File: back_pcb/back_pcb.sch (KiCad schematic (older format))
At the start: 68 parts, among them P1 EXPANSION_LEFT, P2 EXPANSION_BOTTOM, P3 EXPANSION_TOP, P5 AUDIO_CONN, P6 ATMEGA_HEADER, P7 EXPANSION_BOTTOM2, P8 JST, P9 USB_A, Q1 IRLML6401, Q2 IRLML6401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

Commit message: Lots of changes for the Delta revision
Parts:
- removed C15: 100nF, Capacitors_SMD:C_0805_HandSoldering, symbol C_Small
- removed JP5: JUMPER, Connect:GS2, symbol JUMPER
- removed P1: EXPANSION_LEFT, Pin_Headers:Pin_Header_Angled_1x13_Pitch2.54mm, symbol CONN_01X13
- removed P5: AUDIO_CONN, Pin_Headers:Pin_Header_Straight_1x04_Pitch2.54mm, symbol CONN_01X04
- removed W4: TEST_1P, Measurement_Points:Measurement_Point_Square-SMD-Pad_Small, symbol TEST_1P
- added C10, C9: 100nF, common-footprints:C_0805_100nF_HandSoldering, symbol C_Small
- added J1: Conn_01x12, Pin_Headers:Pin_Header_Angled_1x12_Pitch2.54mm, symbol Conn_01x12
- added JP8: WP, common-footprints:GS2_SMALL, symbol JUMPER
- added P4: AUDIO_CONN, Pin_Headers:Pin_Header_Straight_1x06_Pitch2.54mm, symbol CONN_01X06
- added R8: 10K, common-footprints:R_0805_10K_HandSoldering, symbol R
- added U5: 24LC16, Housings_SOIC:SOIC-8_3.9x4.9mm_Pitch1.27mm, symbol 24LC16
- C13, C14, C2, C25, C5, C6, C8: footprint Capacitors_SMD:C_0805_HandSoldering -> common-footprints:C_0805_100nF_HandSoldering
- C4, C7: footprint Capacitors_Tantalum_SMD:CP_Tantalum_Case-B_EIA-3528-21_Hand -> Capacitors_Tantalum_SMD:CP_Tantalum_Case-D_EIA-7343-31_Hand
- P9: symbol USB_A-RESCUE-back_prototype -> USB_A-RESCUE-back_pcb
- R1, R10, R11, R2, R3, R4: footprint Resistors_SMD:R_0805_HandSoldering -> common-footprints:R_0805_10K_HandSoldering
- R5, R6, R7: value 1K -> 47
- U1: footprint common-footprints:pi0outline -> footprints:Pi0-BACK
- U3: symbol MCP23017-RESCUE-back_prototype -> MCP23017-RESCUE-back_pcb
- W25: value TEST_1P -> D-
- W26: value TEST_1P -> D+
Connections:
- net labels added: +3.3VA, AMPLIFIER_ON, BAT_IN+, BAT_IN-
- net labels removed: BATT+, BATT-, IMU_INT, RTC_ALARM
- wire segments 85 -> 99
- no-connect marks 22 -> 24
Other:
- note added: "The board has a cutout,\nyou solder wires from\nthese testpoints to\nPi Zero USB testpoints,\nwires go through\nthe cutout."
- note removed: "The board has a cutout,\nyou solder wires from\nthese testpoints to\nPi USB testpoints,\nwires go through\nthe cutout."
- moved on the sheet: C17, C19, C22, C24, C3, C6, L1, L2, P8, Q2, R4, SW1

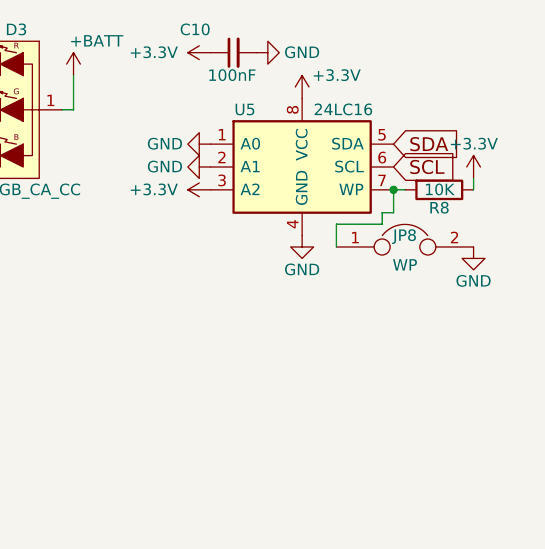
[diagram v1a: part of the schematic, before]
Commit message: Renaming WP (write protect) into WE (write enable)
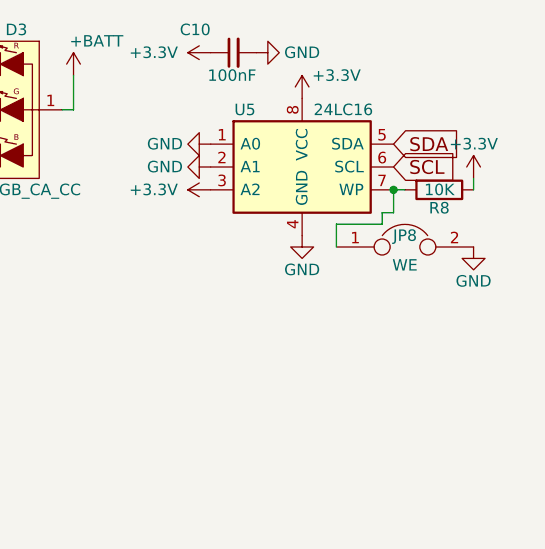
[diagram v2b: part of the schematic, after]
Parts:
- JP8: value WP -> WE
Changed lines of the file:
@@
 P 10800 1450
 F 0 "JP8" H 10800 1500 50  0000 C CNN
-F 1 "WP" H 10800 1370 50  0000 C CNN
+F 1 "WE" H 10800 1370 50  0000 C CNN
 F 2 "common-footprints:GS2_SMALL" H 10800 1450 50  0001 C CNN
 F 3 "" H 10800 1450 50  0000 C CNN

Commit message: More silkscreen changes
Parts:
- Q1, Q2, Q4: footprint TO_SOT_Packages_SMD:SOT-23_Handsoldering -> common-footprints:IRLML6401-SOT-23_Handsoldering
- R5, R6, R7: footprint Resistors_SMD:R_0805_HandSoldering -> common-footprints:R_0805_47R_HandSoldering
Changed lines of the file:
@@
 F 0 "R5" V 8830 650 50  0000 C CNN
 F 1 "47" V 8750 650 50  0000 C CNN
-F 2 "Resistors_SMD:R_0805_HandSoldering" V 8680 650 50  0001 C CNN
+F 2 "common-footprints:R_0805_47R_HandSoldering" V 8680 650 50  0001 C CNN
 F 3 "" H 8750 650 50  0000 C CNN
 	1    8750 650
@@
 F 0 "R6" V 8830 850 50  0000 C CNN
 F 1 "47" V 8750 850 50  0000 C CNN
-F 2 "Resistors_SMD:R_0805_HandSoldering" V 8680 850 50  0001 C CNN
+F 2 "common-footprints:R_0805_47R_HandSoldering" V 8680 850 50  0001 C CNN
 F 3 "" H 8750 850 50  0000 C CNN
 	1    8750 850
@@
 F 0 "R7" V 8830 1050 50  0000 C CNN
 F 1 "47" V 8750 1050 50  0000 C CNN
-F 2 "Resistors_SMD:R_0805_HandSoldering" V 8680 1050 50  0001 C CNN
+F 2 "common-footprints:R_0805_47R_HandSoldering" V 8680 1050 50  0001 C CNN
 F 3 "" H 8750 1050 50  0000 C CNN
 	1    8750 1050
@@
 F 0 "Q1" V 7400 2350 50  0000 R CNN
 F 1 "IRLML6401" V 7650 2350 50  0000 R CNN
-F 2 "TO_SOT_Packages_SMD:SOT-23_Handsoldering" H 7650 2250 50  0001 C CNN
+F 2 "common-footprints:IRLML6401-SOT-23_Handsoldering" H 7650 2250 50  0001 C CNN
 F 3 "" H 7450 2150 50  0000 C CNN
 	1    7450 2150
@@
 F 0 "Q4" V 7850 6500 50  0000 R CNN
 F 1 "IRLML6401" V 8100 6500 50  0000 R CNN
-F 2 "TO_SOT_Packages_SMD:SOT-23_Handsoldering" H 8100 6400 50  0001 C CNN
+F 2 "common-footprints:IRLML6401-SOT-23_Handsoldering" H 8100 6400 50  0001 C CNN
 F 3 "" H 7900 6300 50  0000 C CNN
 	1    7900 6300
@@
 F 0 "Q2" V 7850 3950 50  0000 R CNN
 F 1 "IRLML6401" V 8100 3950 50  0000 R CNN
-F 2 "TO_SOT_Packages_SMD:SOT-23_Handsoldering" H 8100 3850 50  0001 C CNN
+F 2 "common-footprints:IRLML6401-SOT-23_Handsoldering" H 8100 3850 50  0001 C CNN
 F 3 "" H 7900 3750 50  0000 C CNN
 	1    7900 3750

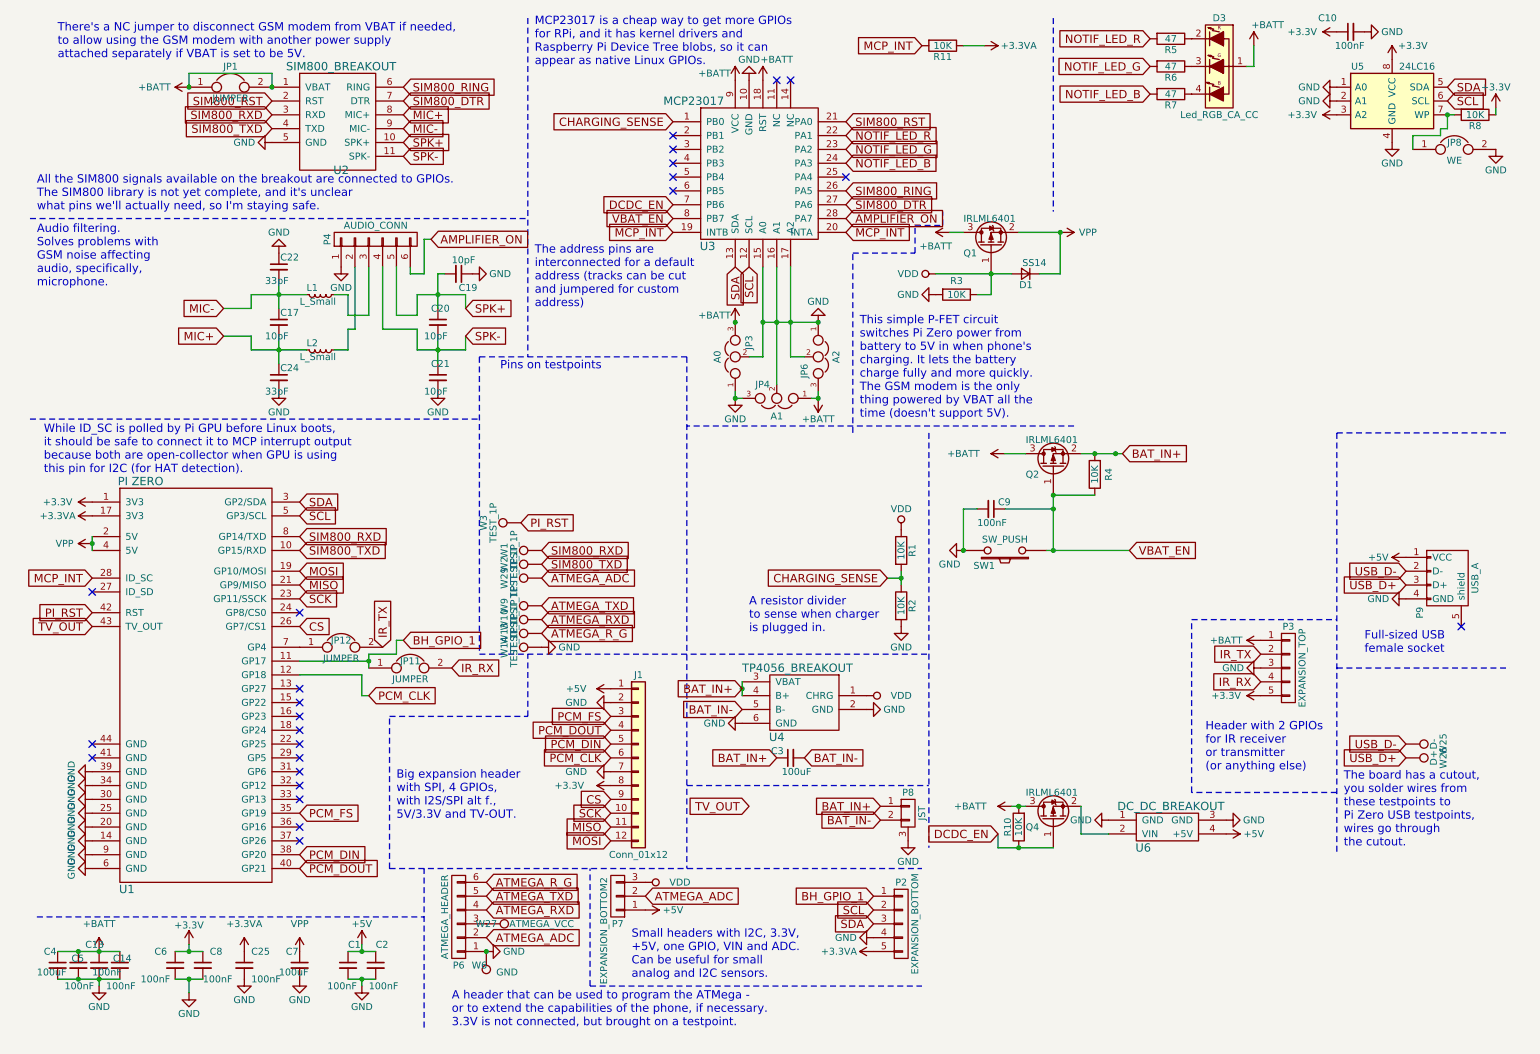
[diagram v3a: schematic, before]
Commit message: Added a UART buffer, TX/RX testpoints, 1N4148 and other silk changes
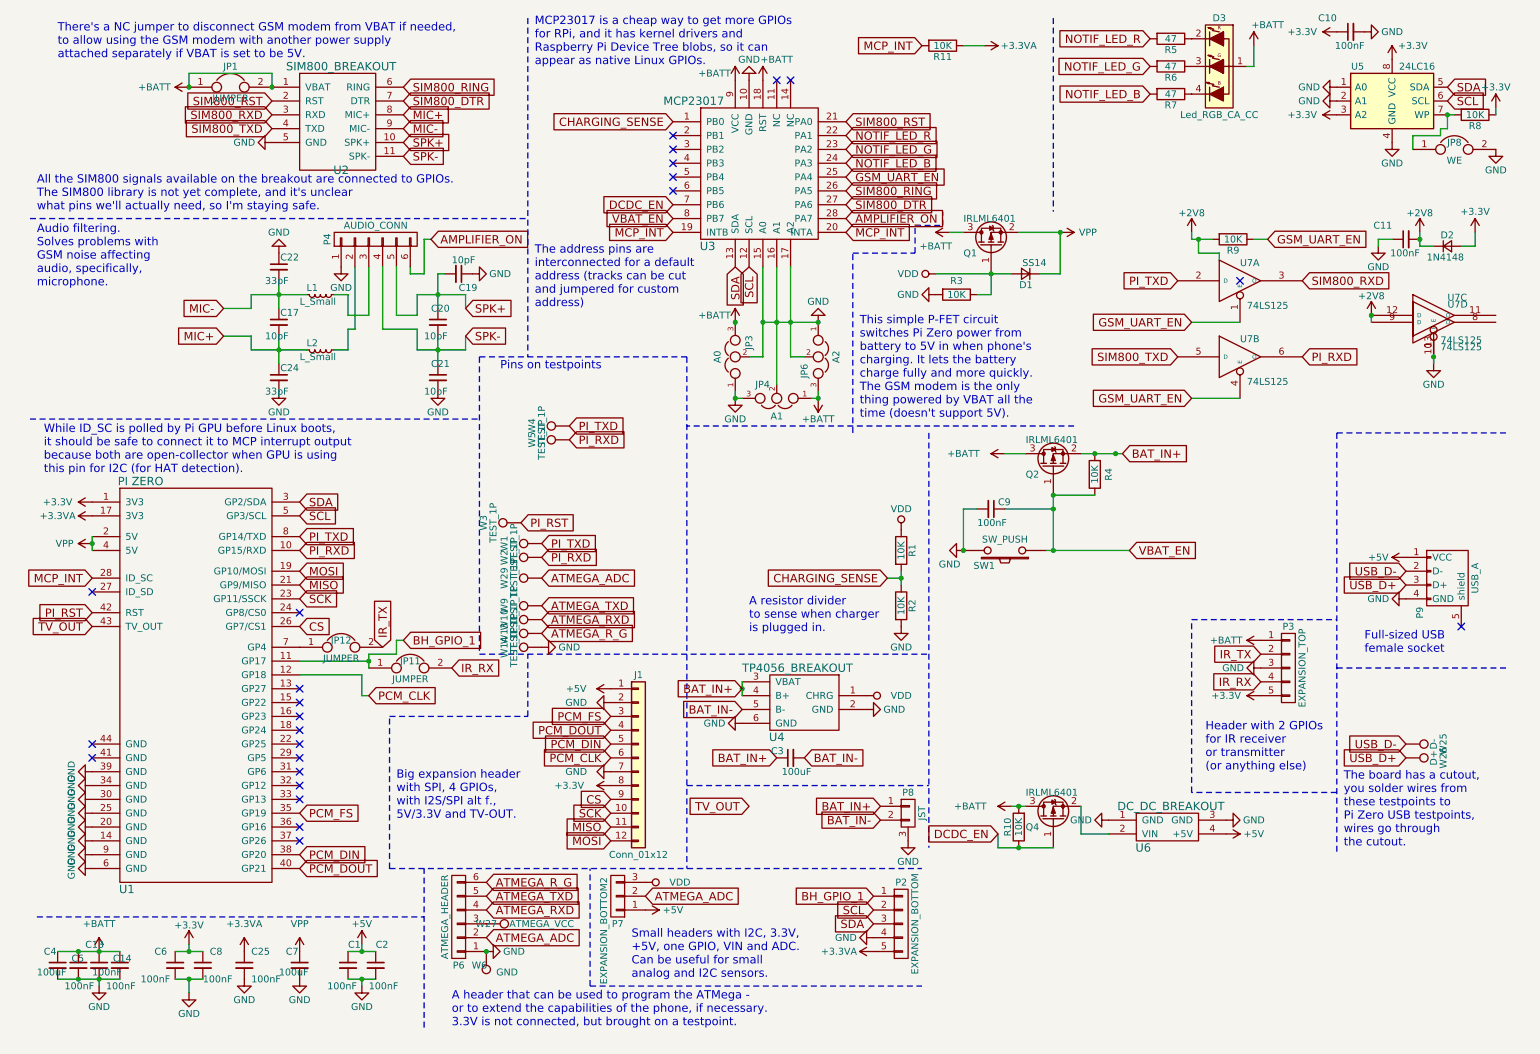
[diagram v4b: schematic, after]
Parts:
- added C11: 100nF, common-footprints:C_0805_100nF_HandSoldering, symbol C_Small
- added D2: 1N4148, common-footprints:1N4148-D_MiniMELF_Handsoldering, symbol D_Small
- added R9: 10K, common-footprints:R_0805_10K_HandSoldering, symbol R
- added U7: 74LS125, Housings_SOIC:SOIC-14_3.9x8.7mm_Pitch1.27mm, symbol 74LS125
- added W4, W5: TEST_1P, Measurement_Points:Measurement_Point_Round-SMD-Pad_Small, symbol TEST_1P
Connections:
- net +3V3: now also D2.2 (A)
- net GND: now also C11.1, U7.10 (E), U7.13 (E), U7.7 (GND), U7.7 (GND), U7.7 (GND), U7.7 (GND)
- net SIM800_RXD: now also U7.3 (O); no longer U1.8 (GP14/TXD), W1.1
- net SIM800_TXD: now also U7.5 (D); no longer U1.10 (GP15/RXD), W2.1
- net GSM_UART_EN: now reaches U3.25 (PA4)
- net GSM_UART_EN: now also R9.1, U7.1 (E), U7.4 (E)
- new net +2V8: C11.2, D2.1 (K), R9.2, U7.12 (D), U7.14 (VCC), U7.14 (VCC), U7.14 (VCC), U7.14 (VCC), U7.9 (D)
- new net PI_RXD: U1.10 (GP15/RXD), U7.6 (O), W2.1, W5.1
- new net PI_TXD: U1.8 (GP14/TXD), U7.2 (D), W1.1, W4.1
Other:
- moved on the sheet: W1, W2

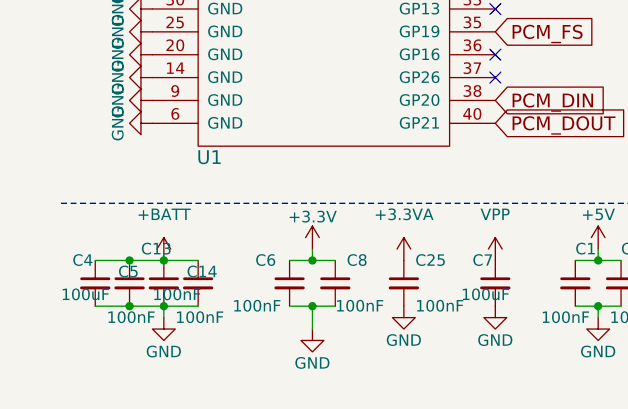
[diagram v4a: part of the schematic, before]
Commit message: Adding 10pF and 33pF caps to modem VBAT
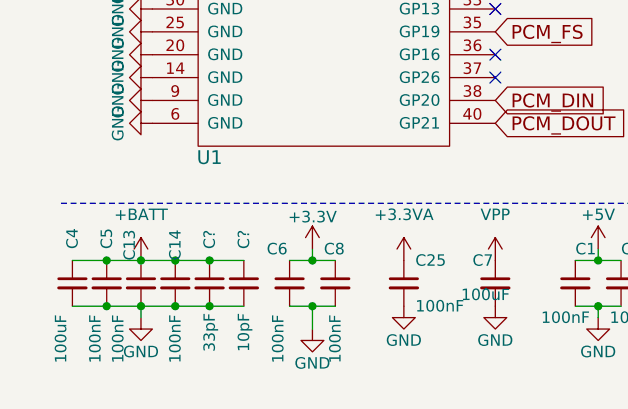
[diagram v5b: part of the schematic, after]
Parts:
- added C?: 33pF, Capacitors_SMD:C_0603_HandSoldering, symbol C_Small
- added C?: 10pF, Capacitors_SMD:C_0603_HandSoldering, symbol C_Small
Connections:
- net +BATT: now also C?.1, C?.1
- net GND: now also C?.2, C?.2
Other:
- moved on the sheet: C13, C14, C4, C5
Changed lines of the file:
@@
 U 1 1 58485760
 P 1550 7350
-F 0 "C6" H 1400 7450 50  0000 L CNN
-F 1 "100nF" H 1300 7250 50  0000 L CNN
+F 0 "C6" H 1450 7500 50  0000 L CNN
+F 1 "100nF" V 1500 7000 50  0000 L CNN
 F 2 "common-footprints:C_0805_100nF_HandSoldering" H 1550 7350 50  0001 C CNN
 F 3 "" H 1550 7350 50  0000 C CNN
@@
 L C_Small C5
 U 1 1 58485DA1
-P 850 7350
-F 0 "C5" H 800 7400 50  0000 L CNN
-F 1 "100nF" H 750 7200 50  0000 L CNN
-F 2 "common-footprints:C_0805_100nF_HandSoldering" H 850 7350 50  0001 C CNN
-F 3 "" H 850 7350 50  0000 C CNN
-	1    850  7350
+P 750 7350
+F 0 "C5" V 750 7500 50  0000 L CNN
+F 1 "100nF" V 700 7000 50  0000 L CNN
+F 2 "common-footprints:C_0805_100nF_HandSoldering" H 750 7350 50  0001 C CNN
+F 3 "" H 750 7350 50  0000 C CNN
+	1    750  7350
 	1    0    0    -1
 $EndComp
@@
 L C_Small C4
 U 1 1 58485E32
-P 700 7350
-F 0 "C4" H 600 7450 50  0000 L CNN
-F 1 "100uF" H 550 7300 50  0000 L CNN
-F 2 "Capacitors_Tantalum_SMD:CP_Tantalum_Case-D_EIA-7343-31_Hand" H 700 7350 50  0001 C CNN
-F 3 "" H 700 7350 50  0000 C CNN
-	1    700  7350
+P 600 7350
+F 0 "C4" V 600 7500 50  0000 L CNN
+F 1 "100uF" V 550 7000 50  0000 L CNN
+F 2 "Capacitors_Tantalum_SMD:CP_Tantalum_Case-D_EIA-7343-31_Hand" H 600 7350 50  0001 C CNN
+F 3 "" H 600 7350 50  0000 C CNN
+	1    600  7350
 	1    0    0    -1
 $EndComp
@@
 U 1 1 58485F63
 P 1750 7350
-F 0 "C8" H 1800 7450 50  0000 L CNN
-F 1 "100nF" H 1750 7250 50  0000 L CNN
+F 0 "C8" H 1700 7500 50  0000 L CNN
+F 1 "100nF" V 1750 7000 50  0000 L CNN
 F 2 "common-footprints:C_0805_100nF_HandSoldering" H 1750 7350 50  0001 C CNN
 F 3 "" H 1750 7350 50  0000 C CNN
@@
 L C_Small C13
 U 1 1 5883ACC8
-P 1000 7350
-F 0 "C13" H 900 7500 50  0000 L CNN
-F 1 "100nF" H 950 7300 50  0000 L CNN
-F 2 "common-footprints:C_0805_100nF_HandSoldering" H 1000 7350 50  0001 C CNN
-F 3 "" H 1000 7350 50  0000 C CNN
-	1    1000 7350
+P 900 7350
+F 0 "C13" V 850 7450 50  0000 L CNN
+F 1 "100nF" V 800 7000 50  0000 L CNN
+F 2 "common-footprints:C_0805_100nF_HandSoldering" H 900 7350 50  0001 C CNN
+F 3 "" H 900 7350 50  0000 C CNN
+	1    900  7350
 	1    0    0    -1
 $EndComp
@@
 L C_Small C14
 U 1 1 58840B61
-P 1150 7350
-F 0 "C14" H 1100 7400 50  0000 L CNN
-F 1 "100nF" H 1050 7200 50  0000 L CNN
-F 2 "common-footprints:C_0805_100nF_HandSoldering" H 1150 7350 50  0001 C CNN
-F 3 "" H 1150 7350 50  0000 C CNN
-	1    1150 7350
+P 1050 7350
+F 0 "C14" V 1050 7450 50  0000 L CNN
+F 1 "100nF" V 1050 7000 50  0000 L CNN
+F 2 "common-footprints:C_0805_100nF_HandSoldering" H 1050 7350 50  0001 C CNN
+F 3 "" H 1050 7350 50  0000 C CNN
+	1    1050 7350
 	1    0    0    -1
 $EndComp
@@
 L +BATT #PWR044
 U 1 1 58911AF4
-P 1000 7250
-F 0 "#PWR044" H 1000 7100 50  0001 C CNN
-F 1 "+BATT" H 1000 7450 50  0000 C CNN
-F 2 "" H 1000 7250 50  0000 C CNN
-F 3 "" H 1000 7250 50  0000 C CNN
-	1    1000 7250
+P 900 7250
+F 0 "#PWR044" H 900 7100 50  0001 C CNN
+F 1 "+BATT" H 900 7450 50  0000 C CNN
+F 2 "" H 900 7250 50  0000 C CNN
+F 3 "" H 900 7250 50  0000 C CNN
+	1    900  7250
 	1    0    0    -1
 $EndComp
@@
 L GND #PWR045
 U 1 1 589168FA
-P 1000 7500
-F 0 "#PWR045" H 1000 7250 50  0001 C CNN
-F 1 "GND" H 1000 7350 50  0000 C CNN
-F 2 "" H 1000 7500 50  0000 C CNN
-F 3 "" H 1000 7500 50  0000 C CNN
-	1    1000 7500
+P 900 7500
+F 0 "#PWR045" H 900 7250 50  0001 C CNN
+F 1 "GND" H 900 7350 50  0000 C CNN
+F 2 "" H 900 7500 50  0000 C CNN
+F 3 "" H 900 7500 50  0000 C CNN
+	1    900  7500
 	1    0    0    -1
 $EndComp
@@
 	9350 850  9350 700
 Connection ~ 7950 2050
-Connection ~ 850  7250
-Connection ~ 850  7450
-Connection ~ 1000 7250
-Connection ~ 1000 7450
+Connection ~ 750  7250
+Connection ~ 750  7450
+Connection ~ 900  7250
+Connection ~ 900  7450
 Wire Wire Line
 	2950 2300 2950 2650
@@
 	8050 3450 5250 3450
 Wire Wire Line
-	1000 7500 1000 7450
-Wire Wire Line
-	700  7250 1150 7250
-Wire Wire Line
-	1150 7450 700  7450
+	900  7500 900  7450
+Wire Wire Line
+	600  7250 1350 7250
+Wire Wire Line
+	600  7450 1350 7450
 Wire Wire Line
 	7900 3950 8200 3950
@@
 PI_RXD
 NoConn ~ 5150 1750
+$Comp
+L C_Small C?
+U 1 1 5A8751CF
+P 1200 7350
+F 0 "C?" V 1200 7500 50  0000 L CNN
+F 1 "33pF" V 1200 7050 50  0000 L CNN
+F 2 "Capacitors_SMD:C_0603_HandSoldering" H 1200 7350 50  0001 C CNN
+F 3 "" H 1200 7350 50  0000 C CNN
+	1    1200 7350
+	1    0    0    -1
+$EndComp
+$Comp
+L C_Small C?
+U 1 1 5A8752DB
+P 1350 7350
+F 0 "C?" V 1350 7500 50  0000 L CNN
+F 1 "10pF" V 1350 7050 50  0000 L CNN
+F 2 "Capacitors_SMD:C_0603_HandSoldering" H 1350 7350 50  0001 C CNN
+F 3 "" H 1350 7350 50  0000 C CNN
+	1    1350 7350
+	1    0    0    -1
+$EndComp
+Connection ~ 1050 7250
+Connection ~ 1200 7250
+Connection ~ 1050 7450
+Connection ~ 1200 7450
 $EndSCHEMATC

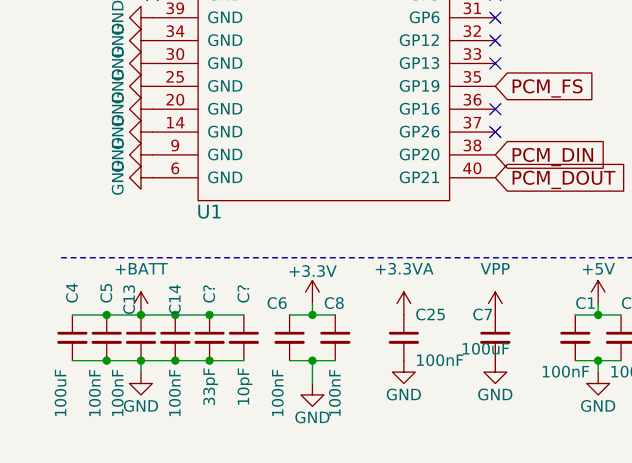
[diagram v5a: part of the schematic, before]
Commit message: Added silkscreen markings for 10pF and 33pF modem VBAT caps
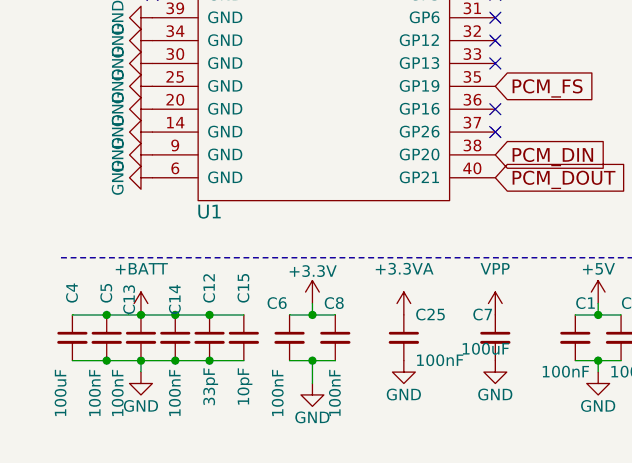
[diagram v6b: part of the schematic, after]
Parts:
- gave numbers to parts that had none: 2

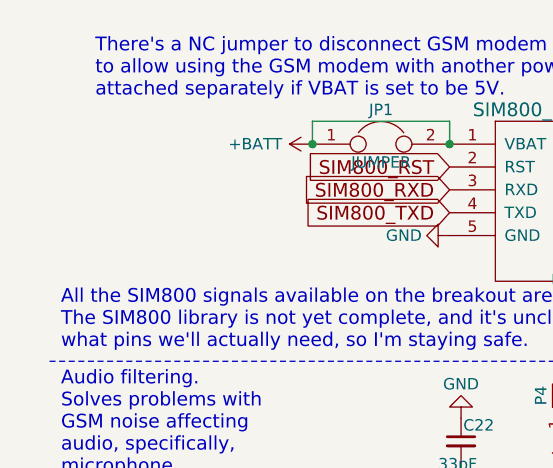
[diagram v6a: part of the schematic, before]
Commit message: Added Zener for modem, silkscreen changes, fill adjustments
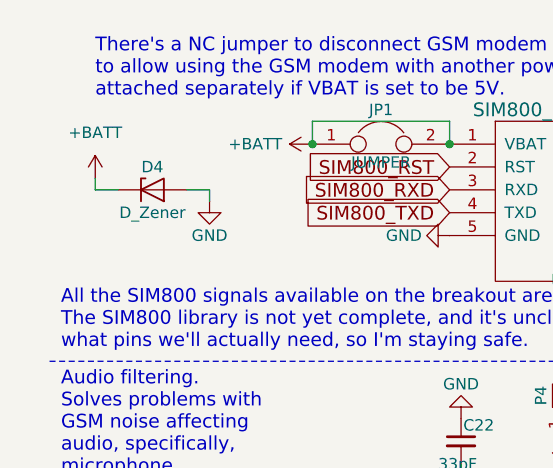
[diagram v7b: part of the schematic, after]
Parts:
- added D4: D_Zener, Resistors_SMD:R_0805_HandSoldering, symbol D_Zener
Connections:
- net +BATT: now also D4.1 (K)
- net GND: now also D4.2 (A)
